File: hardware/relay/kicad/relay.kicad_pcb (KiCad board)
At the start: 4 copper layers, 70 x 45 mm, 12 parts, among them J1 USB4135-GF-A, SW1 BTN1, SW2 BTN2, SW3 BTN3, SW4 BTN4, U1 nRF52840, U2 PN7150, U3 BQ25504, U4 AP2112K-3.3

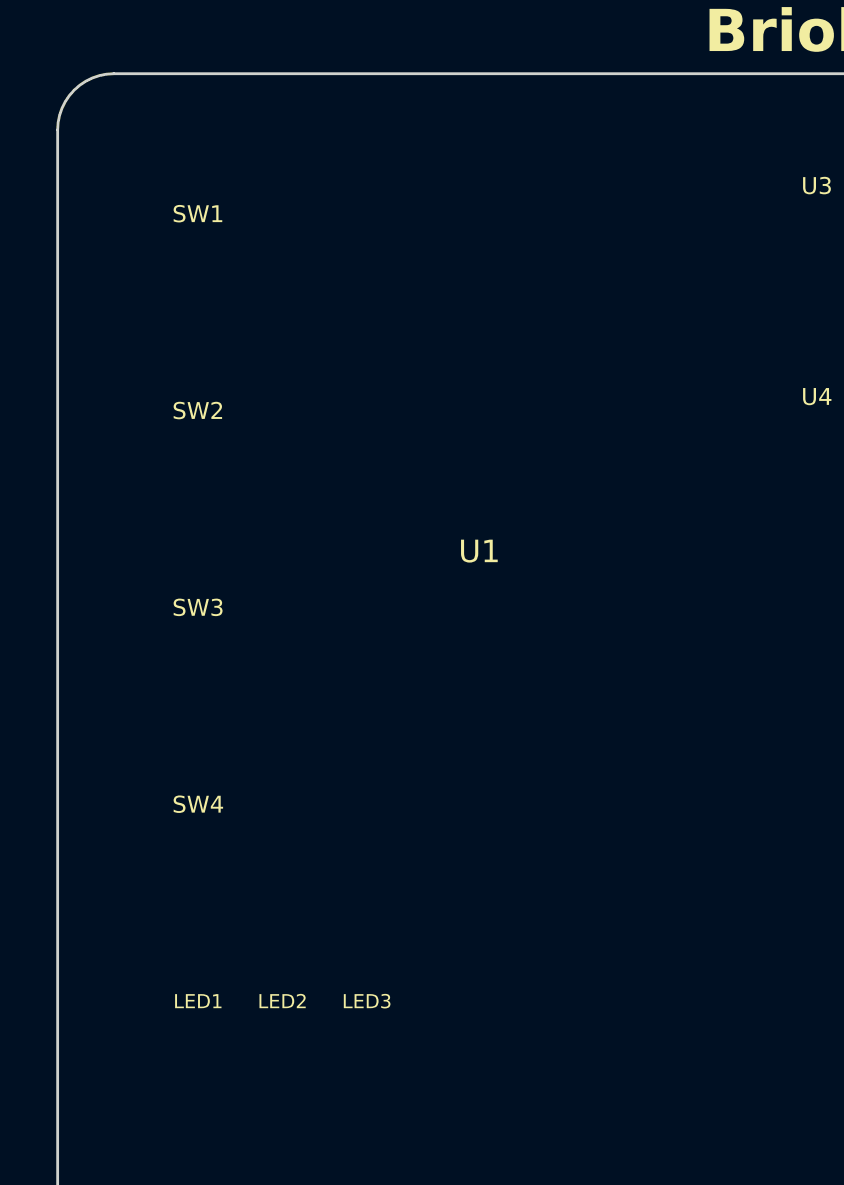
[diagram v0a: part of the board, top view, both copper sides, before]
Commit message: Add 13-key numeric keypad to relay using TCA8418 I2C scanner
Replace 4-button vertical column with full numeric keypad for amount
entry (0-9, decimal, OK, Clear). Uses TCA8418 I2C keypad scanner IC
(WQFN-24, 4x4mm, 3µA standby) sharing the existing I2C bus with the
PN7150 NFC controller.

Hardware changes:
- KiCad: TCA8418 symbol + WQFN-24 footprint + 13 switches in 4x4 grid
- PCB: TCA8418 at (-20,-15), switch grid on left side (6mm pitch)
- Schematic: new Keypad sheet, BTN1-4 replaced with KEY_INT/KEY_RST
- Case: 13 button holes in grid pattern (3 empty positions in col 3)
- BOM: +TCA8418RTWR ($0.75), 4→13 switches, +1 decoupling cap

Firmware:
- New briolette-relay-firmware crate with TCA8418 I2C driver
- AmountEntry state machine: digit accumulation, decimal handling,
  OK to confirm (returns cents), Clear to reset
- 6 unit tests passing (matrix mapping, amount entry, display)

Power impact: +3µA idle (negligible vs 12µA existing baseline).

https://claude.ai/code/session_01TM1rFxbipYtvAkh4Vt7My7
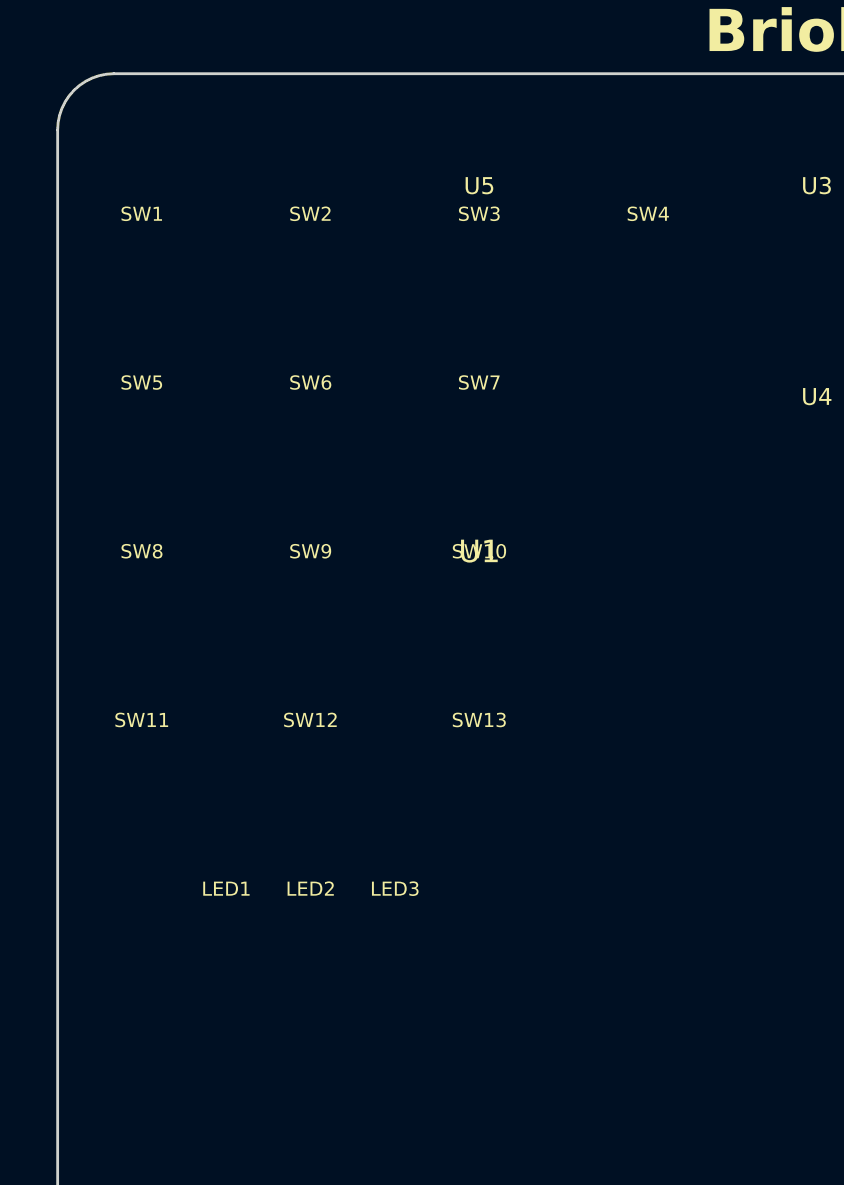
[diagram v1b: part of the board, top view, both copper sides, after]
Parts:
- added SW10: KEY_9, stick-lib:SW_SPST_3x3mm, F.Cu at (-20.0, -3.00)
- added SW11: KEY_DOT, stick-lib:SW_SPST_3x3mm, F.Cu at (-32.0, 3.00)
- added SW12: KEY_0, stick-lib:SW_SPST_3x3mm, F.Cu at (-26.0, 3.00)
- added SW13: KEY_OK, stick-lib:SW_SPST_3x3mm, F.Cu at (-20.0, 3.00)
- added SW5: KEY_4, stick-lib:SW_SPST_3x3mm, F.Cu at (-32.0, -9.00)
- added SW6: KEY_5, stick-lib:SW_SPST_3x3mm, F.Cu at (-26.0, -9.00)
- added SW7: KEY_6, stick-lib:SW_SPST_3x3mm, F.Cu at (-20.0, -9.00)
- added SW8: KEY_7, stick-lib:SW_SPST_3x3mm, F.Cu at (-32.0, -3.00)
- added SW9: KEY_8, stick-lib:SW_SPST_3x3mm, F.Cu at (-26.0, -3.00)
- added U5: TCA8418, relay-lib:WQFN-24-4x4mm, F.Cu at (-20.0, -15.0)
- SW1: value BTN1 -> KEY_1
- SW2: value BTN2 -> KEY_2
- SW3: value BTN3 -> KEY_3
- SW4: value BTN4 -> KEY_CLR
- moved SW4 26.4 mm to (-14.0, -15.0)
- moved SW3 17.2 mm to (-20.0, -15.0)
- moved SW2 8.06 mm to (-26.0, -15.0)
- moved LED1 4.12 mm to (-29.0, 8.00)
- moved LED2 4.12 mm to (-26.0, 8.00)
- moved LED3 4.12 mm to (-23.0, 8.00)
- moved SW1 2.00 mm to (-32.0, -15.0)
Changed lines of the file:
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@@
   (net 7 "NFC_IRQ")
   (net 8 "NFC_VEN")
-  (net 9 "BTN1")
-  (net 10 "BTN2")
-  (net 11 "BTN3")
-  (net 12 "BTN4")
+  (net 9 "KEY_ROW0")
+  (net 10 "KEY_ROW1")
+  (net 11 "KEY_ROW2")
+  (net 12 "KEY_ROW3")
+  (net 24 "KEY_COL0")
+  (net 25 "KEY_COL1")
+  (net 26 "KEY_COL2")
+  (net 27 "KEY_COL3")
+  (net 28 "KEY_INT")
+  (net 29 "KEY_RST")
   (net 13 "LED_R")
   (net 14 "LED_G")
@@
       (effects (font (size 0.8 0.8) (thickness 0.12))))
   )
-  ;; 4 Buttons: left side, vertical column
-  (footprint "stick-lib:SW_SPST_3x3mm" (layer "F.Cu") (at -30.0 -15.0 0)
+  ;; TCA8418 I2C Keypad Scanner (near MCU)
+  (footprint "relay-lib:WQFN-24-4x4mm" (layer "F.Cu") (at -20.0 -15.0 0)
+    (property "Reference" "U5" (at 0 -3.5 0) (layer "F.SilkS")
+      (effects (font (size 0.6 0.6) (thickness 0.1))))
+    (property "Value" "TCA8418" (at 0 3.5 0) (layer "F.Fab")
+      (effects (font (size 0.6 0.6) (thickness 0.1)))))
+  ;; 13-Key Numeric Keypad: 4x4 grid, 6mm pitch
+  ;; Grid origin: X=-32, Y=-15 (top-left of grid)
+  ;; Layout:  1  2  3  CLR
+  ;;          4  5  6  (empty)
+  ;;          7  8  9  (empty)
+  ;;          .  0  OK (empty)
+  ;; Row 0: keys 1, 2, 3, CLR
+  (footprint "stick-lib:SW_SPST_3x3mm" (layer "F.Cu") (at -32.0 -15.0 0)
     (property "Reference" "SW1" (at 0 -2.5 0) (layer "F.SilkS")
-      (effects (font (size 0.6 0.6) (thickness 0.1))))
-    (property "Value" "BTN1" (at 0 2.5 0) (layer "F.Fab")
-      (effects (font (size 0.6 0.6) (thickness 0.1)))))
-  (footprint "stick-lib:SW_SPST_3x3mm" (layer "F.Cu") (at -30.0 -8.0 0)
+      (effects (font (size 0.5 0.5) (thickness 0.08))))
+    (property "Value" "KEY_1" (at 0 2.5 0) (layer "F.Fab")
+      (effects (font (size 0.5 0.5) (thickness 0.08)))))
+  (footprint "stick-lib:SW_SPST_3x3mm" (layer "F.Cu") (at -26.0 -15.0 0)
     (property "Reference" "SW2" (at 0 -2.5 0) (layer "F.SilkS")
-      (effects (font (size 0.6 0.6) (thickness 0.1))))
-    (property "Value" "BTN2" (at 0 2.5 0) (layer "F.Fab")
-      (effects (font (size 0.6 0.6) (thickness 0.1)))))
-  (footprint "stick-lib:SW_SPST_3x3mm" (layer "F.Cu") (at -30.0 -1.0 0)
+      (effects (font (size 0.5 0.5) (thickness 0.08))))
+    (property "Value" "KEY_2" (at 0 2.5 0) (layer "F.Fab")
+      (effects (font (size 0.5 0.5) (thickness 0.08)))))
+  (footprint "stick-lib:SW_SPST_3x3mm" (layer "F.Cu") (at -20.0 -15.0 0)
     (property "Reference" "SW3" (at 0 -2.5 0) (layer "F.SilkS")
-      (effects (font (size 0.6 0.6) (thickness 0.1))))
-    (property "Value" "BTN3" (at 0 2.5 0) (layer "F.Fab")
-      (effects (font (size 0.6 0.6) (thickness 0.1)))))
-  (footprint "stick-lib:SW_SPST_3x3mm" (layer "F.Cu") (at -30.0 6.0 0)
+      (effects (font (size 0.5 0.5) (thickness 0.08))))
+    (property "Value" "KEY_3" (at 0 2.5 0) (layer "F.Fab")
+      (effects (font (size 0.5 0.5) (thickness 0.08)))))
+  (footprint "stick-lib:SW_SPST_3x3mm" (layer "F.Cu") (at -14.0 -15.0 0)
     (property "Reference" "SW4" (at 0 -2.5 0) (layer "F.SilkS")
-      (effects (font (size 0.6 0.6) (thickness 0.1))))
-    (property "Value" "BTN4" (at 0 2.5 0) (layer "F.Fab")
-      (effects (font (size 0.6 0.6) (thickness 0.1)))))
-  ;; 3 LEDs: near buttons
-  (footprint "LED_SMD:LED_0402_1005Metric" (layer "F.Cu") (at -30.0 12.0 0)
+      (effects (font (size 0.5 0.5) (thickness 0.08))))
+    (property "Value" "KEY_CLR" (at 0 2.5 0) (layer "F.Fab")
+      (effects (font (size 0.5 0.5) (thickness 0.08)))))
+  ;; Row 1: keys 4, 5, 6
+  (footprint "stick-lib:SW_SPST_3x3mm" (layer "F.Cu") (at -32.0 -9.0 0)
+    (property "Reference" "SW5" (at 0 -2.5 0) (layer "F.SilkS")
+      (effects (font (size 0.5 0.5) (thickness 0.08))))
+    (property "Value" "KEY_4" (at 0 2.5 0) (layer "F.Fab")
+      (effects (font (size 0.5 0.5) (thickness 0.08)))))
+  (footprint "stick-lib:SW_SPST_3x3mm" (layer "F.Cu") (at -26.0 -9.0 0)
+    (property "Reference" "SW6" (at 0 -2.5 0) (layer "F.SilkS")
+      (effects (font (size 0.5 0.5) (thickness 0.08))))
+    (property "Value" "KEY_5" (at 0 2.5 0) (layer "F.Fab")
+      (effects (font (size 0.5 0.5) (thickness 0.08)))))
+  (footprint "stick-lib:SW_SPST_3x3mm" (layer "F.Cu") (at -20.0 -9.0 0)
+    (property "Reference" "SW7" (at 0 -2.5 0) (layer "F.SilkS")
+      (effects (font (size 0.5 0.5) (thickness 0.08))))
+    (property "Value" "KEY_6" (at 0 2.5 0) (layer "F.Fab")
+      (effects (font (size 0.5 0.5) (thickness 0.08)))))
+  ;; Row 2: keys 7, 8, 9
+  (footprint "stick-lib:SW_SPST_3x3mm" (layer "F.Cu") (at -32.0 -3.0 0)
+    (property "Reference" "SW8" (at 0 -2.5 0) (layer "F.SilkS")
+      (effects (font (size 0.5 0.5) (thickness 0.08))))
+    (property "Value" "KEY_7" (at 0 2.5 0) (layer "F.Fab")
+      (effects (font (size 0.5 0.5) (thickness 0.08)))))
+  (footprint "stick-lib:SW_SPST_3x3mm" (layer "F.Cu") (at -26.0 -3.0 0)
+    (property "Reference" "SW9" (at 0 -2.5 0) (layer "F.SilkS")
+      (effects (font (size 0.5 0.5) (thickness 0.08))))
+    (property "Value" "KEY_8" (at 0 2.5 0) (layer "F.Fab")
+      (effects (font (size 0.5 0.5) (thickness 0.08)))))
+  (footprint "stick-lib:SW_SPST_3x3mm" (layer "F.Cu") (at -20.0 -3.0 0)
+    (property "Reference" "SW10" (at 0 -2.5 0) (layer "F.SilkS")
+      (effects (font (size 0.5 0.5) (thickness 0.08))))
+    (property "Value" "KEY_9" (at 0 2.5 0) (layer "F.Fab")
+      (effects (font (size 0.5 0.5) (thickness 0.08)))))
+  ;; Row 3: keys ., 0, OK
+  (footprint "stick-lib:SW_SPST_3x3mm" (layer "F.Cu") (at -32.0 3.0 0)
+    (property "Reference" "SW11" (at 0 -2.5 0) (layer "F.SilkS")
+      (effects (font (size 0.5 0.5) (thickness 0.08))))
+    (property "Value" "KEY_DOT" (at 0 2.5 0) (layer "F.Fab")
+      (effects (font (size 0.5 0.5) (thickness 0.08)))))
+  (footprint "stick-lib:SW_SPST_3x3mm" (layer "F.Cu") (at -26.0 3.0 0)
+    (property "Reference" "SW12" (at 0 -2.5 0) (layer "F.SilkS")
+      (effects (font (size 0.5 0.5) (thickness 0.08))))
+    (property "Value" "KEY_0" (at 0 2.5 0) (layer "F.Fab")
+      (effects (font (size 0.5 0.5) (thickness 0.08)))))
+  (footprint "stick-lib:SW_SPST_3x3mm" (layer "F.Cu") (at -20.0 3.0 0)
+    (property "Reference" "SW13" (at 0 -2.5 0) (layer "F.SilkS")
+      (effects (font (size 0.5 0.5) (thickness 0.08))))
+    (property "Value" "KEY_OK" (at 0 2.5 0) (layer "F.Fab")
+      (effects (font (size 0.5 0.5) (thickness 0.08)))))
+  ;; 3 LEDs: above keypad grid
+  (footprint "LED_SMD:LED_0402_1005Metric" (layer "F.Cu") (at -29.0 8.0 0)
     (property "Reference" "LED1" (at 0 -1.5 0) (layer "F.SilkS")
       (effects (font (size 0.5 0.5) (thickness 0.08))))
     (property "Value" "RED" (at 0 1.5 0) (layer "F.Fab")
       (effects (font (size 0.5 0.5) (thickness 0.08)))))
-  (footprint "LED_SMD:LED_0402_1005Metric" (layer "F.Cu") (at -27.0 12.0 0)
+  (footprint "LED_SMD:LED_0402_1005Metric" (layer "F.Cu") (at -26.0 8.0 0)
     (property "Reference" "LED2" (at 0 -1.5 0) (layer "F.SilkS")
       (effects (font (size 0.5 0.5) (thickness 0.08))))
     (property "Value" "GREEN" (at 0 1.5 0) (layer "F.Fab")
       (effects (font (size 0.5 0.5) (thickness 0.08)))))
-  (footprint "LED_SMD:LED_0402_1005Metric" (layer "F.Cu") (at -24.0 12.0 0)
+  (footprint "LED_SMD:LED_0402_1005Metric" (layer "F.Cu") (at -23.0 8.0 0)
     (property "Reference" "LED3" (at 0 -1.5 0) (layer "F.SilkS")
       (effects (font (size 0.5 0.5) (thickness 0.08))))
